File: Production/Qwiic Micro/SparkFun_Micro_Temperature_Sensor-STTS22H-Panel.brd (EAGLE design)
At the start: 78.2 x 174.5 mm, 2229 parts, among them J1 Qwiic Right Angle, J10 Qwiic Right Angle, J100 Qwiic Right Angle, J103 Qwiic Right Angle, J106 Qwiic Right Angle, J109 Qwiic Right Angle, J112 Qwiic Right Angle, J115 Qwiic Right Angle, J118 Qwiic Right Angle, J121 Qwiic Right Angle, J124 Qwiic Right Angle, J127 Qwiic Right Angle, J13 Qwiic Right Angle, J130 Qwiic Right Angle, J133 Qwiic Right Angle, J136 Qwiic Right Angle, J139 Qwiic Right Angle, J142 Qwiic Right Angle, J145 Qwiic Right Angle, J148 Qwiic Right Angle, J151 Qwiic Right Angle, J154 Qwiic Right Angle, J157 Qwiic Right Angle, J16 Qwiic Right Angle, J160 Qwiic Right Angle, J163 Qwiic Right Angle, J166 Qwiic Right Angle, J169 Qwiic Right Angle, J19 Qwiic Right Angle, J2 Qwiic Right Angle, J22 Qwiic Right Angle, J25 Qwiic Right Angle, J28 Qwiic Right Angle, J31 Qwiic Right Angle, J34 Qwiic Right Angle, J37 Qwiic Right Angle, J40 Qwiic Right Angle, J43 Qwiic Right Angle, J46 Qwiic Right Angle, J49 Qwiic Right Angle, J52 Qwiic Right Angle, J55 Qwiic Right Angle, J58 Qwiic Right Angle, J61 Qwiic Right Angle, J64 Qwiic Right Angle, J67 Qwiic Right Angle, J7 Qwiic Right Angle, J70 Qwiic Right Angle, J73 Qwiic Right Angle, J76 Qwiic Right Angle, J79 Qwiic Right Angle, J82 Qwiic Right Angle, J85 Qwiic Right Angle, J88 Qwiic Right Angle, J91 Qwiic Right Angle, J94 Qwiic Right Angle, J97 Qwiic Right Angle, U1 STTS22H, U10 STTS22H, U11 STTS22H, U12 STTS22H, U13 STTS22H, U14 STTS22H, U15 STTS22H, U16 STTS22H, U17 STTS22H, U18 STTS22H, U19 STTS22H, U2 STTS22H, U20 STTS22H, U21 STTS22H, U22 STTS22H, U23 STTS22H, U24 STTS22H, U25 STTS22H, U26 STTS22H, U27 STTS22H, U28 STTS22H, U29 STTS22H, U3 STTS22H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

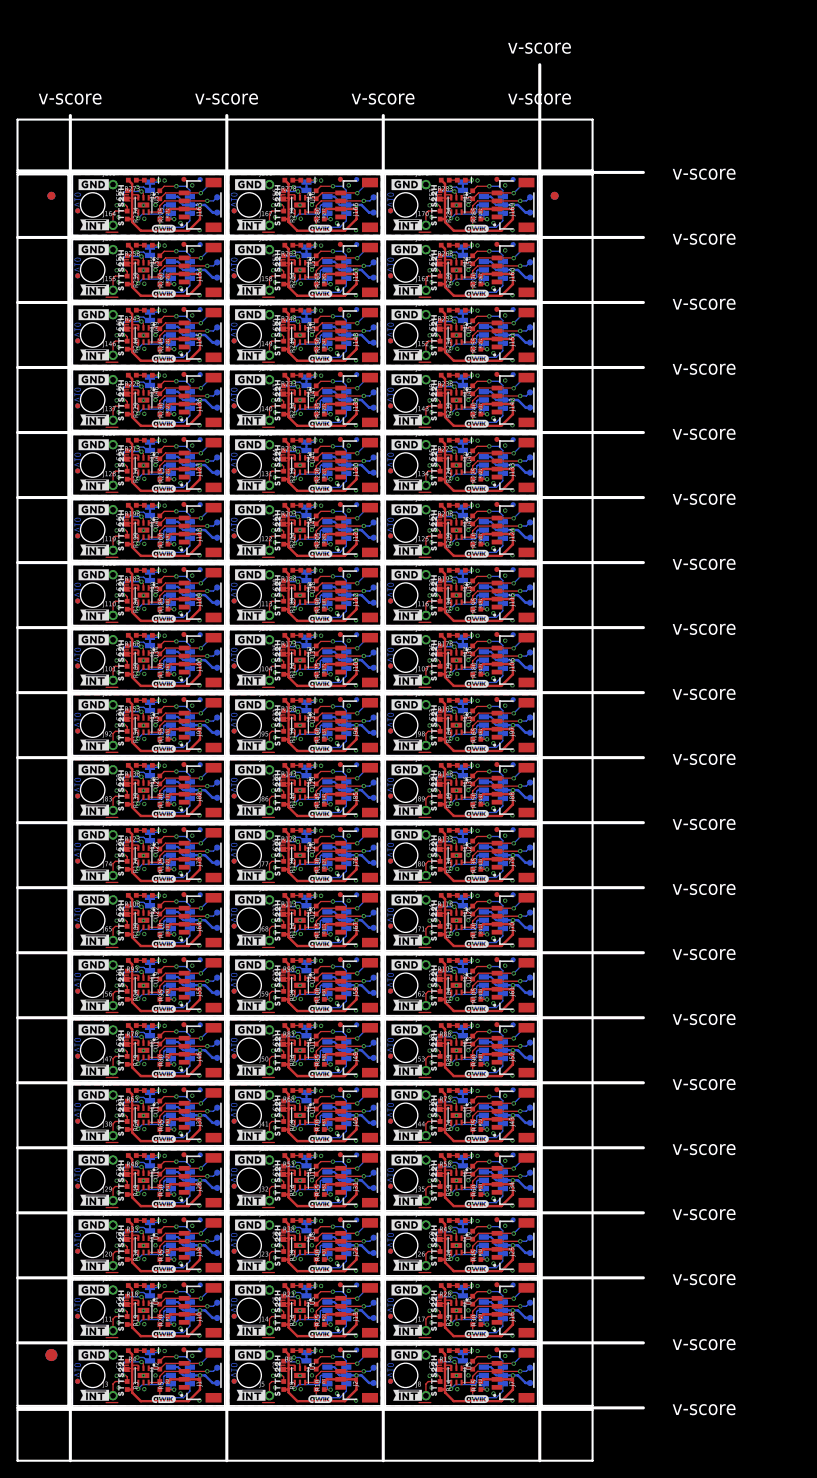
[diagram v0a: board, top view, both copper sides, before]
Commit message: Re-panelizes Qwiic Micro
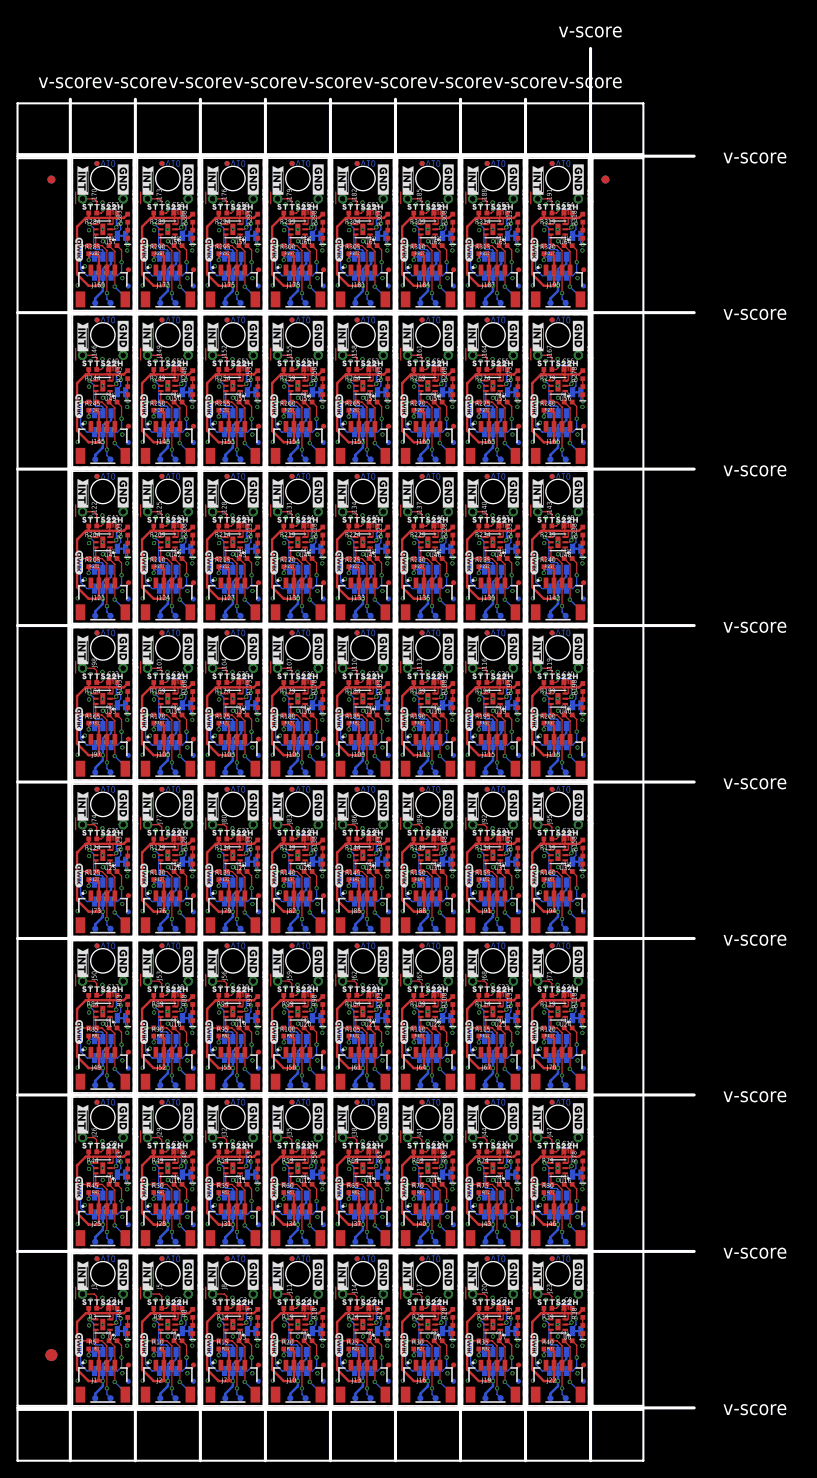
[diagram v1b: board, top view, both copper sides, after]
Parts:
- added ADDR57, ADDR58, ADDR59, ADDR60, ADDR61, ADDR62, ADDR63: JUMPER-SMT_3_1-NC_TRACE_SILK, SparkFun-Jumpers:SMT-JUMPER_3_1-NC_TRACE_SILK
- added C58, C59, C60, C61, C62, C63, C64: 0.1uF, SparkFun-Capacitors:0402-TIGHT
- added D58, D59, D60, D61, D62, D63, D64: RED, SparkFun-LED:LED-0402
- added FD115, FD116, FD117, FD118, FD119, FD120, FD121, FD122, FD123, FD124, FD125, FD126, FD127, FD128, FID115, FID116, FID117, FID118, FID119, FID120, FID121, FID122, FID123, FID124, FID125, FID126, FID127, FID128: FIDUCIALUFIDUCIAL, SparkFun-Aesthetics:FIDUCIAL-MICRO
- added I2C_PU57, I2C_PU58, I2C_PU59, I2C_PU60, I2C_PU61, I2C_PU62, I2C_PU63: S_MODE, SparkFun-Jumpers:SMT-JUMPER_3_2-NC_TRACE_SILK
- added J172, J175, J178, J181, J184, J187, J190: Qwiic Right Angle, SparkFun-Connectors:JST04_1MM_RA
- added J173, J174, J176, J177, J179, J180, J182, J183, J185, J186, J188, J189, J191, J192: (no value), SparkFun-Connectors:1X01_1MM_NO_SILK
- added LED57, LED58, LED59, LED60, LED61, LED62, LED63: JUMPER-SMT_2_NC_TRACE_SILK, SparkFun-Jumpers:SMT-JUMPER_2_NC_TRACE_SILK
- added LOGO172, LOGO175, LOGO178, LOGO181, LOGO184, LOGO187, LOGO190: OSHW-LOGOMINI, SparkFun-Aesthetics:OSHW-LOGO-MINI
- added LOGO173, LOGO176, LOGO179, LOGO182, LOGO185, LOGO188, LOGO191: QWIIC_LOGO_3MM, SparkFun-Aesthetics:QWIIC_3MM
- added LOGO174, LOGO177, LOGO180, LOGO183, LOGO186, LOGO189, LOGO192: SFE_LOGO_NAME_FLAMEBLANK, SparkFun-Aesthetics:BLANK
- added R286, R287, R288, R291, R292, R293, R296, R297, R298, R301, R302, R303, R306, R307, R308, R311, R312, R313, R316, R317, R318: 2.2k, SparkFun-Resistors:0402-TIGHT
- added R289, R294, R299, R304, R309, R314, R319: 10k, SparkFun-Resistors:0402-TIGHT
- added R290, R295, R300, R305, R310, R315, R320: 15K, SparkFun-Resistors:0402-TIGHT
- added STANDOFF58, STANDOFF59, STANDOFF60, STANDOFF61, STANDOFF62, STANDOFF63, STANDOFF64: STAND-OFFTIGHT, SparkFun-Hardware:STAND-OFF-TIGHT
- added TP229, TP230, TP231, TP232, TP233, TP234, TP235, TP236, TP237, TP238, TP239, TP240, TP241, TP242, TP243, TP244, TP245, TP246, TP247, TP248, TP249, TP250, TP251, TP252, TP253, TP254, TP255, TP256: TEST-POINT3, SparkFun-Connectors:PAD.03X.03
- added U$742, U$755, U$768, U$781, U$794, U$807, U$820: (no value), SparkFun-Aesthetics:SFE_LOGO_FLAME_.1
- added U$743, U$756, U$769, U$782, U$795, U$808, U$821: (no value), ISMTopMini:#LED#2121
- added U$744, U$757, U$770, U$783, U$796, U$809, U$822: (no value), top:#0#4
- added U$745, U$758, U$771, U$784, U$797, U$810, U$823: (no value), top:#1#4
- added U$746, U$759, U$772, U$785, U$798, U$811, U$824: (no value), top:#I2C#4
- added U$747, U$748, U$760, U$761, U$773, U$774, U$786, U$787, U$799, U$800, U$812, U$813, U$825, U$826: (no value), top:#GND#4
- added U$749, U$762, U$775, U$788, U$801, U$814, U$827: (no value), bot:##INT##9
- added U$750, U$763, U$776, U$789, U$802, U$815, U$828: (no value), top:##INT##9
- added U$751, U$752, U$764, U$765, U$777, U$778, U$790, U$791, U$803, U$804, U$816, U$817, U$829, U$830: (no value), bot:STTS22H11
- added U$753, U$766, U$779, U$792, U$805, U$818, U$831: (no value), bot:TEMP24
- added U$754, U$767, U$780, U$793, U$806, U$819, U$832: (no value), bot:SENSOR25
- added U58, U59, U60, U61, U62, U63, U64: STTS22H, STTS22H:UDFN-6L
- moved LOGO120 63.2 mm to (17.5, 63.0)
- moved U$513 63.0 mm to (63.2, 94.6), turned to 270 degrees
- moved U$514 63.0 mm to (63.2, 94.6), turned to 90 degrees
- moved U$201 61.6 mm to (63.2, 35.9), turned to 270 degrees
- moved U$202 61.6 mm to (63.2, 35.9), turned to 90 degrees
- moved J120 61.4 mm to (63.2, 92.2), turned to 270 degrees
- moved R198 60.7 mm to (63.8, 89.8), turned to 90 degrees
- moved LOGO48 60.7 mm to (17.5, 4.32)
- moved FD80 60.5 mm to (60.0, 96.6), turned to 90 degrees
- moved FID80 60.5 mm to (60.0, 96.6), turned to 270 degrees
- moved U$509 60.1 mm to (63.2, 89.9), turned to 90 degrees
- moved STANDOFF40 60.0 mm to (60.7, 94.7), turned to 270 degrees
- moved J48 59.7 mm to (63.2, 33.5), turned to 270 degrees
- moved D40 59.7 mm to (63.8, 87.8), turned to 270 degrees
- moved FD32 59.6 mm to (60.0, 37.9), turned to 90 degrees
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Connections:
- new net !INT!57: J173.1, R289.1, U58.P2
- new net !INT!58: J176.1, R294.1, U59.P2
- new net !INT!59: J179.1, R299.1, U60.P2
- new net !INT!60: J182.1, R304.1, U61.P2
- new net !INT!61: J185.1, R309.1, U62.P2
- new net !INT!62: J188.1, R314.1, U63.P2
- new net !INT!63: J191.1, R319.1, U64.P2
- new net 3.3V57: ADDR57.1, C58.1, I2C_PU57.2, J172.2, R288.2, R289.2, R290.2, TP231.1, U58.P3
- new net 3.3V58: ADDR58.1, C59.1, I2C_PU58.2, J175.2, R293.2, R294.2, R295.2, TP235.1, U59.P3
- new net 3.3V59: ADDR59.1, C60.1, I2C_PU59.2, J178.2, R298.2, R299.2, R300.2, TP239.1, U60.P3
- new net 3.3V60: ADDR60.1, C61.1, I2C_PU60.2, J181.2, R303.2, R304.2, R305.2, TP243.1, U61.P3
- new net 3.3V61: ADDR61.1, C62.1, I2C_PU61.2, J184.2, R308.2, R309.2, R310.2, TP247.1, U62.P3
- new net 3.3V62: ADDR62.1, C63.1, I2C_PU62.2, J187.2, R313.2, R314.2, R315.2, TP251.1, U63.P3
- new net 3.3V63: ADDR63.1, C64.1, I2C_PU63.2, J190.2, R318.2, R319.2, R320.2, TP255.1, U64.P3
- new net ADDR57: ADDR57.2, U58.P4
- new net ADDR58: ADDR58.2, U59.P4
- new net ADDR59: ADDR59.2, U60.P4
- new net ADDR60: ADDR60.2, U61.P4
- new net ADDR61: ADDR61.2, U62.P4
- new net ADDR62: ADDR62.2, U63.P4
- new net ADDR63: ADDR63.2, U64.P4
- new net GND57: C58.2, J172.1, J174.1, LED57.1, TP232.1, U58.P5, U58.P7
- new net GND58: C59.2, J175.1, J177.1, LED58.1, TP236.1, U59.P5, U59.P7
- new net GND59: C60.2, J178.1, J180.1, LED59.1, TP240.1, U60.P5, U60.P7
- new net GND60: C61.2, J181.1, J183.1, LED60.1, TP244.1, U61.P5, U61.P7
- new net GND61: C62.2, J184.1, J186.1, LED61.1, TP248.1, U62.P5, U62.P7
- new net GND62: C63.2, J187.1, J189.1, LED62.1, TP252.1, U63.P5, U63.P7
- new net GND63: C64.2, J190.1, J192.1, LED63.1, TP256.1, U64.P5, U64.P7
- new net N$286: I2C_PU57.1, R286.2
- new net N$287: I2C_PU57.3, R287.2
- new net N$288: D58.A, R288.1
- new net N$289: D58.C, LED57.2
- new net N$290: ADDR57.3, R290.1
- new net N$291: I2C_PU58.1, R291.2
- new net N$292: I2C_PU58.3, R292.2
- new net N$293: D59.A, R293.1
- new net N$294: D59.C, LED58.2
- new net N$295: ADDR58.3, R295.1
- new net N$296: I2C_PU59.1, R296.2
- new net N$297: I2C_PU59.3, R297.2
- new net N$298: D60.A, R298.1
- new net N$299: D60.C, LED59.2
- new net N$300: ADDR59.3, R300.1
- new net N$301: I2C_PU60.1, R301.2
- new net N$302: I2C_PU60.3, R302.2
- new net N$303: D61.A, R303.1
- new net N$304: D61.C, LED60.2
- new net N$305: ADDR60.3, R305.1
- new net N$306: I2C_PU61.1, R306.2
- new net N$307: I2C_PU61.3, R307.2
- new net N$308: D62.A, R308.1
- new net N$309: D62.C, LED61.2
- new net N$310: ADDR61.3, R310.1
- new net N$311: I2C_PU62.1, R311.2
- new net N$312: I2C_PU62.3, R312.2
- new net N$313: D63.A, R313.1
- new net N$314: D63.C, LED62.2
- new net N$315: ADDR62.3, R315.1
- new net N$316: I2C_PU63.1, R316.2
- new net N$317: I2C_PU63.3, R317.2
- new net N$318: D64.A, R318.1
- new net N$319: D64.C, LED63.2
- new net N$320: ADDR63.3, R320.1
- new net SCL57: J172.4, R286.1, TP229.1, U58.P1
- new net SCL58: J175.4, R291.1, TP233.1, U59.P1
- new net SCL59: J178.4, R296.1, TP237.1, U60.P1
- new net SCL60: J181.4, R301.1, TP241.1, U61.P1
- new net SCL61: J184.4, R306.1, TP245.1, U62.P1
- new net SCL62: J187.4, R311.1, TP249.1, U63.P1
- new net SCL63: J190.4, R316.1, TP253.1, U64.P1
- new net SDA57: J172.3, R287.1, TP230.1, U58.P6
- new net SDA58: J175.3, R292.1, TP234.1, U59.P6
- new net SDA59: J178.3, R297.1, TP238.1, U60.P6
- new net SDA60: J181.3, R302.1, TP242.1, U61.P6
- new net SDA61: J184.3, R307.1, TP246.1, U62.P6
- new net SDA62: J187.3, R312.1, TP250.1, U63.P6
- new net SDA63: J190.3, R317.1, TP254.1, U64.P6
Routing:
- net 3.3V57: track 0.00 -> 29.3 mm, vias 0 -> 1
- net 3.3V63: track 0.00 -> 29.3 mm, vias 0 -> 1
- net 3.3V62: track 0.00 -> 29.3 mm, vias 0 -> 1
- net 3.3V61: track 0.00 -> 29.3 mm, vias 0 -> 1
- net 3.3V60: track 0.00 -> 29.3 mm, vias 0 -> 1
- net 3.3V59: track 0.00 -> 29.3 mm, vias 0 -> 1
- net 3.3V58: track 0.00 -> 29.3 mm, vias 0 -> 1
- net SDA59: track 0.00 -> 9.70 mm, vias 0 -> 1
- net SDA58: track 0.00 -> 9.70 mm, vias 0 -> 1
- net SDA62: track 0.00 -> 9.70 mm, vias 0 -> 1
- net SDA61: track 0.00 -> 9.70 mm, vias 0 -> 1
- net SDA60: track 0.00 -> 9.70 mm, vias 0 -> 1
- net SDA57: track 0.00 -> 9.70 mm, vias 0 -> 1
- net SDA63: track 0.00 -> 9.70 mm, vias 0 -> 1
- net SCL63: track 0.00 -> 9.52 mm, vias 0 -> 1
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- added copper zone on layer 1, net 3.3V57
- added copper zone on layer 1, net 3.3V58
- added copper zone on layer 1, net 3.3V59
- added copper zone on layer 1, net 3.3V60
- added copper zone on layer 1, net 3.3V61
- added copper zone on layer 1, net 3.3V62
- added copper zone on layer 1, net 3.3V63
- added copper zone on layer 1, net GND57
- added copper zone on layer 16, net GND57
- added copper zone on layer 1, net GND58
- added copper zone on layer 16, net GND58
- added copper zone on layer 1, net GND59
- added copper zone on layer 16, net GND59
- added copper zone on layer 1, net GND60
- added copper zone on layer 16, net GND60
- added copper zone on layer 1, net GND61
- added copper zone on layer 16, net GND61
- added copper zone on layer 1, net GND62
- added copper zone on layer 16, net GND62
- added copper zone on layer 1, net GND63
- added copper zone on layer 16, net GND63
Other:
- board size 78.2 x 174.5 mm -> 84.6 x 176.5 mm
